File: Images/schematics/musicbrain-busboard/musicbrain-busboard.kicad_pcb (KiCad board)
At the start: 2 copper layers, 200 x 115 mm, 24 parts, among them J1 SLOT 1, J2 SLOT 2, J3 SLOT 3, J4 SLOT 4, J5 SLOT 5, J6 SLOT 6, J7 HUB 1, J8 HUB 2, J9 PWR IN, U1 Teensy 4.1, U2 R-78E5.0-0.5, U3 AMS1117-3.3

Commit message: Busboard PCB volledig geroute (DRC 0 fouten, 0 unconnected)
- 28 B.Cu-buslanen (SPI/LDAC/I2C/SPARE/CS1-8/IRQ1-6/voeding), taps per slot
  via kanaal tussen de slots (geografische CS/IRQ per slot)
- Teensy 4.1 fan-out met 33R serieweerstanden inline (R1/R2) en I2C-pullups
- hubs J7/J8 met eigen fans; J8 verplaatst naar zuidkant (planaire routing)
- Eurorack-voeding via mid-row oversteek onder de Teensy-kolommen;
  R-78E (+5V) en AMS1117 (+3V3) aangesloten; ontkoppelrij gevoed
- GND via solide vlakken F+B met 15 stitching-via's
- 502 sporen/via's, programmatisch gegenereerd en met DRC geverifieerd

Co-Authored-By: Claude Fable 5 <noreply@anthropic.com>
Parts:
- moved R3 80.6 mm to (92.0, 104.0)
- moved R4 80.6 mm to (92.0, 107.0)
- moved R1 43.0 mm to (53.0, 73.0)
- moved R2 38.8 mm to (49.5, 71.8), turned to 180 degrees
- moved J8 32.0 mm to (193.0, 104.0)
- moved U2 3.61 mm to (62.0, 108.0)
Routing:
- net +12V: track 0.00 -> 750.5 mm, vias 0 -> 10
- net -12V: track 0.00 -> 677.9 mm, vias 0 -> 10
- net +3V3: track 0.00 -> 636.5 mm, vias 0 -> 11
- net /SCLK: track 0.00 -> 461.0 mm, vias 0 -> 9
- net /MISO: track 0.00 -> 438.6 mm, vias 0 -> 9
- net /MOSI: track 0.00 -> 418.7 mm, vias 0 -> 9
- net /SCL: track 0.00 -> 336.8 mm, vias 0 -> 8
- net /SDA: track 0.00 -> 310.7 mm, vias 0 -> 8
- net /LDAC: track 0.00 -> 285.7 mm, vias 0 -> 7
- net /CS7: track 0.00 -> 282.3 mm, vias 0 -> 2
- net /SPARE2: track 0.00 -> 269.8 mm, vias 0 -> 7
- net /SPARE1: track 0.00 -> 255.0 mm, vias 0 -> 7
- net /CS6: track 0.00 -> 239.2 mm, vias 0 -> 2
- net /CS8: track 0.00 -> 229.6 mm, vias 0 -> 2
- net /CS5: track 0.00 -> 214.1 mm, vias 0 -> 2
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
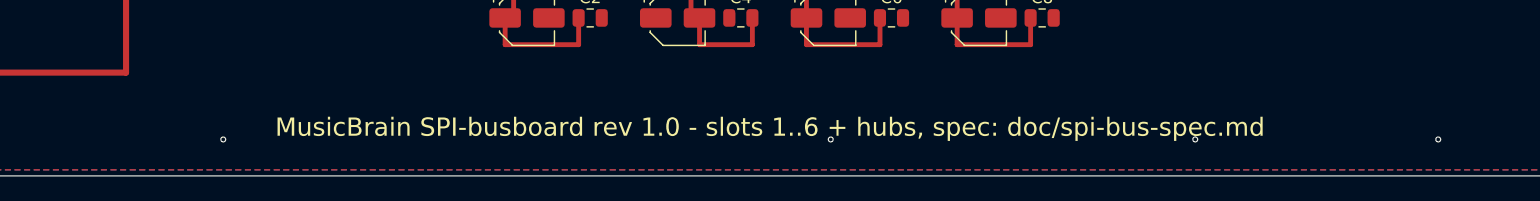
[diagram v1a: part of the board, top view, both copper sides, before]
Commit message: Jack-printjes (jack8/jack4) + mechanica-standaard + silk-links
- jack8/jack4: Thonkiconn (PJ398SM) paneeldragers, sch+PCB volledig geroute
  (ERC 0, DRC 0/0); footprint naar clacktronics/AudioJacks-maten
  (T -4.92 / TN +3.38 / S +6.48, ovale sleufgaten 1.6x0.6)
- 1xN-contract identiek aan GATE8/ADC8-J2; female socket op achterzijde,
  headerhart op 44mm-standaard; TN-normalling via soldeerjumper JP1
  (dicht=inputs, OPEN bij outputs)
- spec: mechanica-standaard (haakse busconnector, frontconnector op 44mm,
  silk-linkschema musicbrain.nl/hw/<bord>); GATE8/ADC8 v1.1 volgt
- silk-links op gate8- en busboard-PCB bijgewerkt (DRC her-geverifieerd 0/0)

Co-Authored-By: Claude Fable 5 <noreply@anthropic.com>
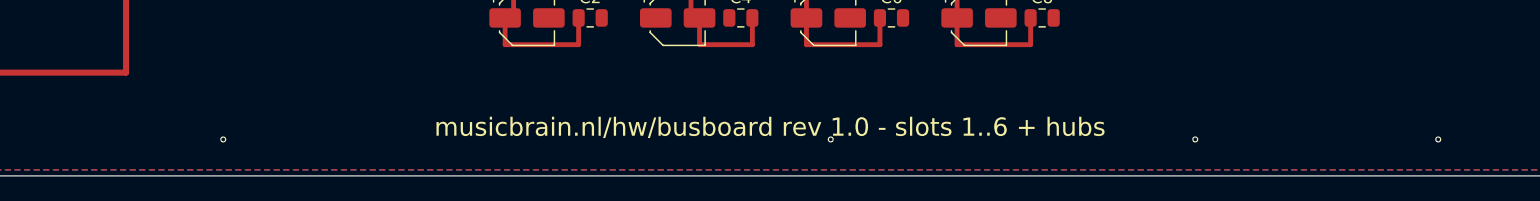
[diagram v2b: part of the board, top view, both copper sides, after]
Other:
- board text added: "musicbrain.nl/hw/busboard rev 1.0 - slots 1..6 + hubs"
- board text removed: "MusicBrain SPI-busboard rev 1.0 - slots 1..6 + hubs, spec: doc/spi-bus-spec.md"
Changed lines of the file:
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@@
     (stroke (width 0.1) (type default)) (fill none)
     (layer "Edge.Cuts"))
-  (gr_text "MusicBrain SPI-busboard rev 1.0 - slots 1..6 + hubs, spec: doc/spi-bus-spec.md" (at 115 121 0) (layer "F.SilkS")
+  (gr_text "musicbrain.nl/hw/busboard rev 1.0 - slots 1..6 + hubs" (at 115 121 0) (layer "F.SilkS")
     (effects (font (size 1.5 1.5) (thickness 0.25))))
   (zone (net 5) (net_name "GND") (layer "F.Cu")

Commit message: Busboard v1.1: EXP-header, display-header (SPI1), Qwiic, M3-gaten
- J10 EXP (2x7): 8 vrije GPIO (D14-D17/D20-D23, analoog + Serial3/4/5)
  + 3V3/5V/GND; signalen via B.Cu-tussenrijlanen west van de Teensy
- J11 DISPLAY (1x9): eigen SPI1, pinvolgorde = ILI9341-module 1-op-1
  (CS=0, RESET=25, DC=24, MOSI1=26, SCK1=27, SDO nc)
- J12 QWIIC (1x4): GND/3V3/SDA/SCL op de bus-I2C, tussen slot 5 en 6
- 5x M3-montagegat voor standoffs (kast + bovenplaat)
- spec bijgewerkt: kaartstatussen v1.1, DAC8 bevestigd, RK097N-potten,
  display/EXP/Qwiic zoals gebouwd, mechanica-sectie 'dragen en geleiden'
  (slot + bovenplaat + standoffs; geen aparte printgeleiders nodig),
  encoderadvies Bourns PEC11R
- ERC 0, netlijst pad-voor-pad geverifieerd, DRC 0/0 (579 route-items)

Co-Authored-By: Claude Fable 5 <noreply@anthropic.com>
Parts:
- added H1: M3, MountingHole:MountingHole_3.2mm_M3, F.Cu at (18.0, 13.0)
- added H2: M3, MountingHole:MountingHole_3.2mm_M3, F.Cu at (115.0, 13.0)
- added H3: M3, MountingHole:MountingHole_3.2mm_M3, F.Cu at (212.0, 13.0)
- added H4: M3, MountingHole:MountingHole_3.2mm_M3, F.Cu at (60.0, 122.0)
- added H5: M3, MountingHole:MountingHole_3.2mm_M3, F.Cu at (140.0, 122.0)
- added J10: EXP, Connector_PinHeader_2.54mm:PinHeader_2x07_P2.54mm_Vertical, F.Cu at (16.6, 27.5)
- added J11: DISPLAY, Connector_PinHeader_2.54mm:PinHeader_1x09_P2.54mm_Vertical, F.Cu at (33.0, 20.0)
- added J12: QWIIC, Connector_PinHeader_2.54mm:PinHeader_1x04_P2.54mm_Vertical, F.Cu at (165.8, 121.5)
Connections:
- U1 pad 16: (no net) -> /DISP_DC
- U1 pad 17: (no net) -> /DISP_RST
- U1 pad 18: (no net) -> /MOSI1
- U1 pad 19: (no net) -> /SCK1
- U1 pad 2: (no net) -> /DISP_CS
- U1 pad 36: (no net) -> /D14
- U1 pad 37: (no net) -> /D15
- U1 pad 38: (no net) -> /D16
- U1 pad 39: (no net) -> /D17
- U1 pad 42: (no net) -> /D20
- U1 pad 43: (no net) -> /D21
- U1 pad 44: (no net) -> /D22
- U1 pad 45: (no net) -> /D23
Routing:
- net +3V3: track 636.5 -> 870.9 mm, vias 11 -> 15
- net +5V: track 197.7 -> 303.7 mm, vias 4 -> 5
- net /SCK1: track 0.00 -> 94.0 mm, vias 0 -> 1
- net /MOSI1: track 0.00 -> 90.5 mm, vias 0 -> 1
- net /DISP_RST: track 0.00 -> 86.1 mm, vias 0 -> 1
- net /DISP_DC: track 0.00 -> 84.5 mm, vias 0 -> 1
- net /D14: track 0.00 -> 77.5 mm
- net /D16: track 0.00 -> 69.9 mm
- net /D15: track 0.00 -> 63.4 mm
- net /D20: track 0.00 -> 57.2 mm
- net /D17: track 0.00 -> 55.8 mm
- net /DISP_CS: track 0.00 -> 52.4 mm, vias 0 -> 1
- net /D22: track 0.00 -> 49.6 mm
- net /SDA: track 310.7 -> 356.6 mm, vias 8 -> 9
- net /SCL: track 336.8 -> 381.4 mm, vias 8 -> 9
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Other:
- board text added: "musicbrain.nl/hw/busboard rev 1.1 - slots 1..6 + hubs + exp/display/qwiic"
- board text removed: "musicbrain.nl/hw/busboard rev 1.0 - slots 1..6 + hubs"
